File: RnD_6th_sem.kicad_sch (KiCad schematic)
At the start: 62 parts, among them IC1 2EDF7275KXUMA1, J1 HVDC, J10 MMCX-J-P-H-ST-TH1, J2 PWM, J3 HVDC, J4 Conn_02x05_Odd_Even, J5 5V, J6 5V, J7 GND, J8 GND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

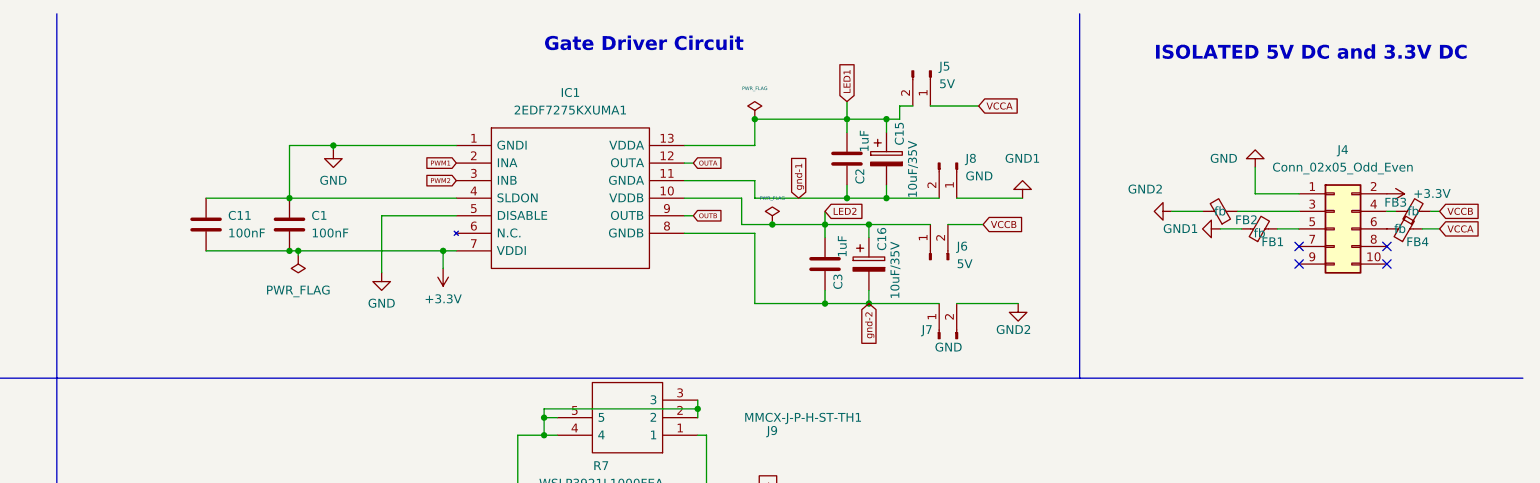
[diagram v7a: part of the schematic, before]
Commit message: updated the layout of FB and caps
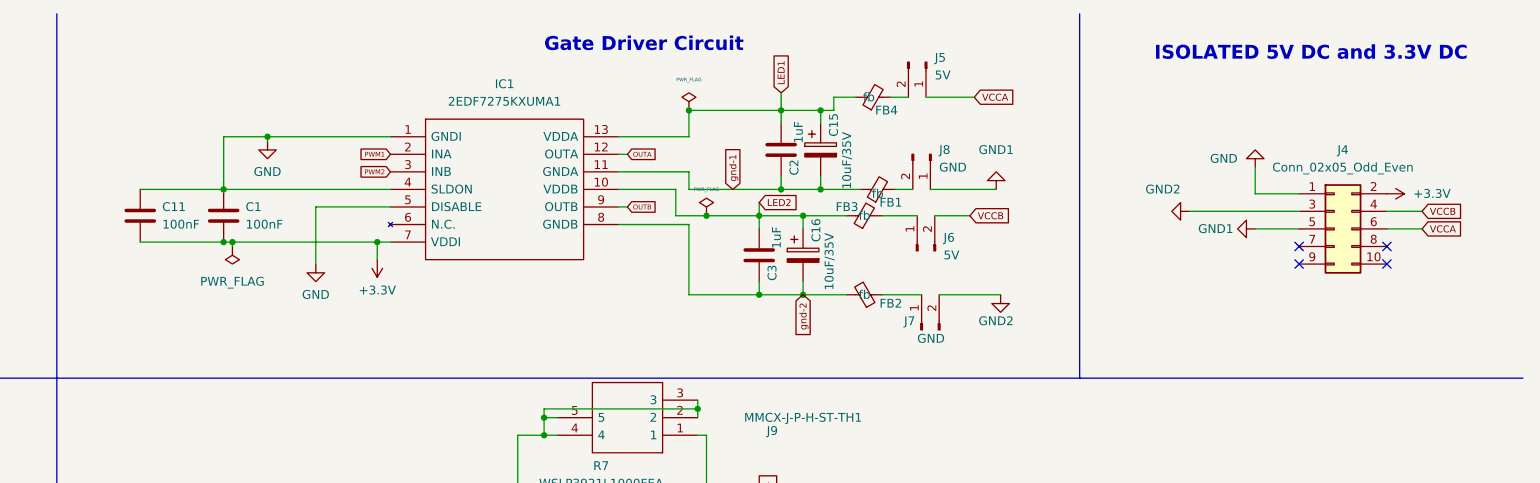
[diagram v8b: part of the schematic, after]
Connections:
- net GND1: now also J4.5 (Pin_5); no longer FB1.1
- net GND2: now also J4.3 (Pin_3); no longer FB2.2
- net LED1: now also FB4.1; no longer J5.2 (Pin_2)
- net LED2: now also FB3.1; no longer J6.1 (Pin_1)
- net VCCA: now also J4.6 (Pin_6); no longer FB4.2
- net VCCB: now also J4.4 (Pin_4); no longer FB3.2
- net gnd-1: now also FB1.1; no longer J8.2 (Pin_2)
- net gnd-2: now also FB2.2; no longer J7.1 (Pin_1)
- net at FB2.1: now also J7.1 (Pin_1); no longer J4.3 (Pin_3)
- net at FB1.2: now also J8.2 (Pin_2); no longer J4.5 (Pin_5)
- new net: FB4.2, J5.2 (Pin_2)
- new net: FB3.2, J6.1 (Pin_1)
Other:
- moved on the sheet: C1, C11, C15, C16, C2, C3, FB1, FB2, FB3, FB4, IC1, J5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
